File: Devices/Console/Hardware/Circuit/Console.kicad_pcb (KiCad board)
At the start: 2 copper layers, 30 parts, among them J1 AVR-ISP-6, J2 TYPE-C-31-M-12, J3 Conn_01x13, J4 Conn_01x04, J5 Conn_01x04, SW1 PEC11R-4220F-S0012, SW2 PEC11R-4220F-S0012, SW3 PEC11R-4220F-S0012, SW4 PEC11R-4220F-S0012, SW5 SW_Push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

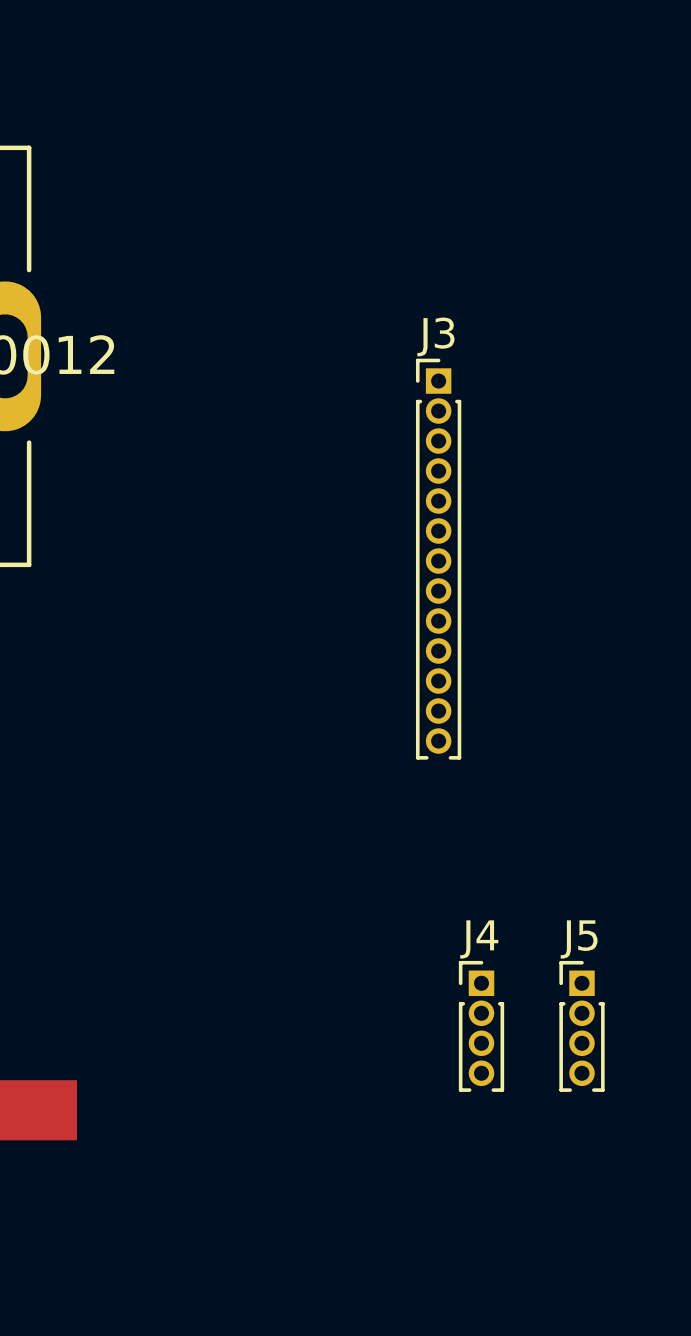
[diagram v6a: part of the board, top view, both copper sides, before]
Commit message: Change pin header size
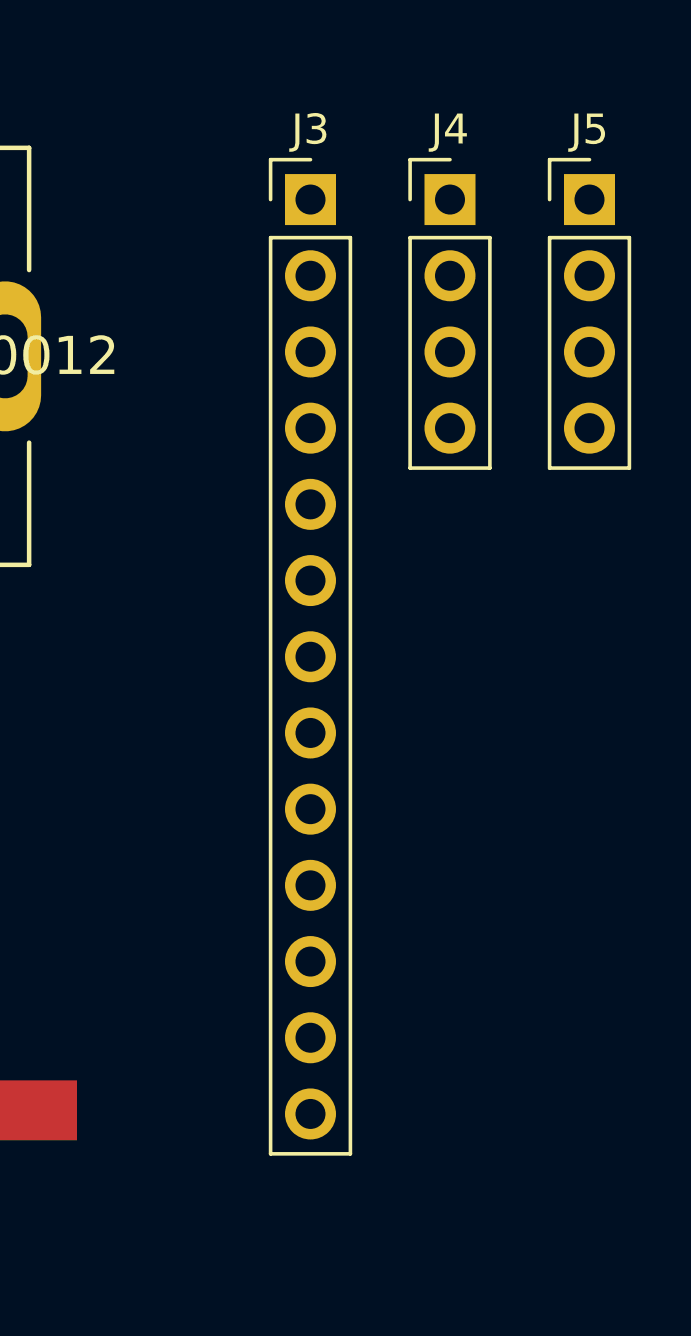
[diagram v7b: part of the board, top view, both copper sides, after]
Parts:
- J3: footprint Connector_PinHeader_1.00mm:PinHeader_1x13_P1.00mm_Vertical -> Connector_PinHeader_2.54mm:PinHeader_1x13_P2.54mm_Vertical
- J4, J5: footprint Connector_PinHeader_1.00mm:PinHeader_1x04_P1.00mm_Vertical -> Connector_PinHeader_2.54mm:PinHeader_1x04_P2.54mm_Vertical
- moved J4 26.1 mm to (159.6, 29.3)
- moved J5 26.1 mm to (164.3, 29.3)
- moved J3 7.40 mm to (155.0, 29.3)

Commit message: First console PCB layout
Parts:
- moved SW5 108.0 mm to (183.6, 48.5)
- moved J5 81.0 mm to (99.1, 77.2)
- moved SW4 78.8 mm to (180.3, 101.6)
- moved SW3 73.9 mm to (154.9, 101.6)
- moved SW2 70.2 mm to (129.5, 101.6)
- moved SW1 68.1 mm to (104.1, 101.6)
- moved J4 65.6 mm to (99.1, 54.4)
- moved JP5 55.8 mm to (133.9, 47.6), turned to 180 degrees
- moved JP2 54.3 mm to (128.1, 52.1), turned to 180 degrees
- moved JP6 48.1 mm to (133.9, 52.1), turned to 180 degrees
- moved R1 47.7 mm to (154.7, 69.1)
- moved C3 46.6 mm to (136.8, 81.0)
- moved JP3 44.0 mm to (157.0, 47.6), turned to 180 degrees
- moved JP9 41.3 mm to (128.1, 47.6), turned to 180 degrees
- moved JP4 40.6 mm to (122.4, 47.6), turned to 180 degrees
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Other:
- board outline added: 96.8 x 74.4 mm
- board text added: "RST"
- board text added: "RX"
- board text added: "SCL"
- board text added: "SDA"
- board text added: "TX"
